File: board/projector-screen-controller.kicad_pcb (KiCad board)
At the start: 2 copper layers, 97.2 x 106 mm, 63 parts, among them J1 ICSP, J2 MSTBVA-3-G, J3 MCV-3-G, J4 MCV-3-G, J5 MCV-3-G, J6 MSTBVA-6-G, J7 MCV-3-G, K1 JS1-12V-F, K2 JS1-12V-F, K3 JS1-12V-F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

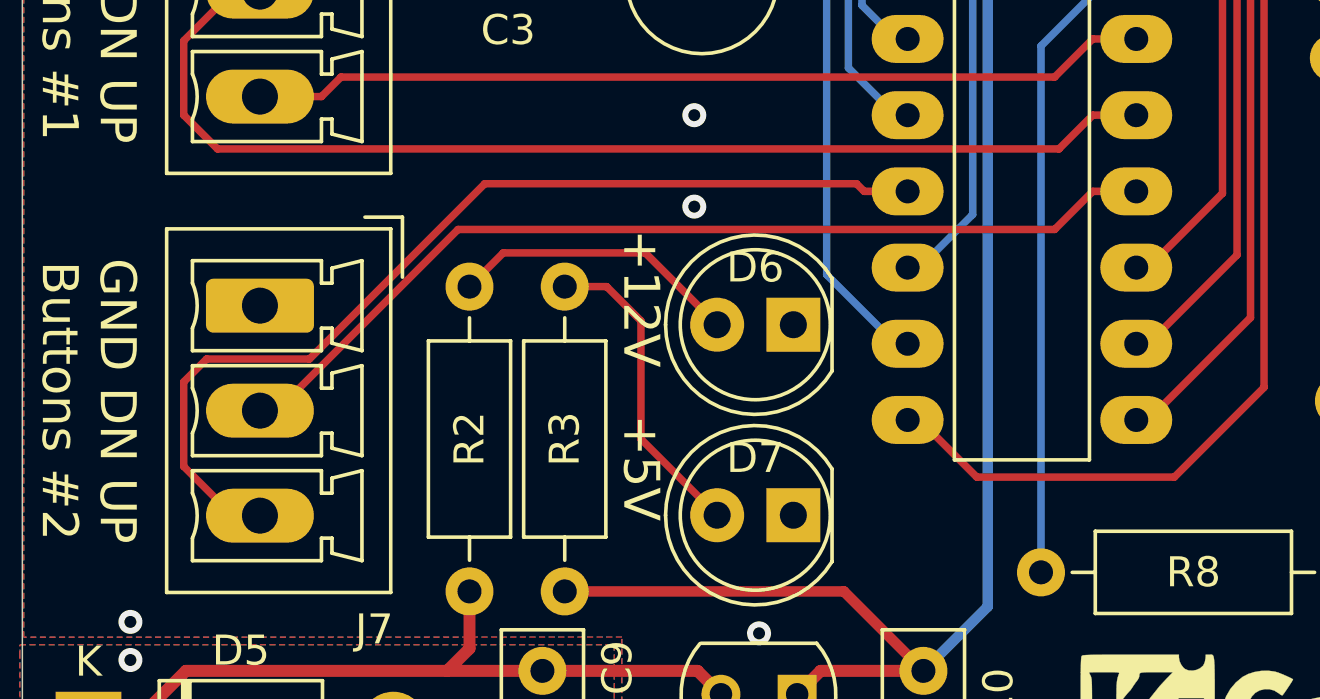
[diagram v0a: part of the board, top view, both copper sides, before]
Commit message: Fix channel 2 button reversal
* The hierarchical schematic pins for channel 2 buttons were reversed in the
  root schematic. Correct this, and add board revision logic to the firmware so
  board versions can be targeted by the build.
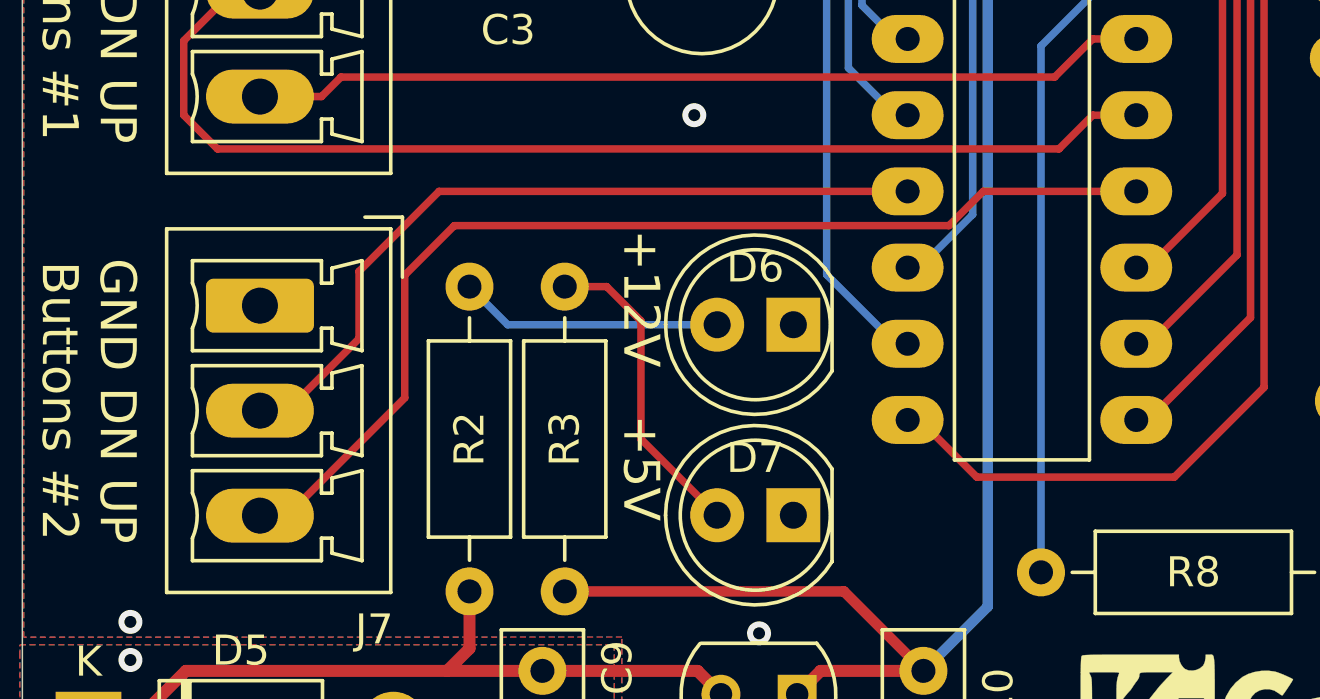
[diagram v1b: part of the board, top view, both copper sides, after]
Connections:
- J7 pad 2: /MCU/BUT2_UP -> /MCU/BUT2_DN
- J7 pad 3: /MCU/BUT2_DN -> /MCU/BUT2_UP
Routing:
- net /MCU/BUT2_DN: track 33.0 -> 25.9 mm
- net /MCU/BUT2_UP: track 32.2 -> 36.1 mm
- net Net-(D6-Pad2): track 9.71 -> 8.78 mm
- net GND: vias 12 -> 11
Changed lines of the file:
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@@
-(kicad_pcb (version 20171130) (host pcbnew "(5.1.4-0-10_14)")
+(kicad_pcb (version 20171130) (host pcbnew "(5.1.4)-1")
   (general
     (thickness 1.6)
     (drawings 91)
-    (tracks 381)
+    (tracks 377)
     (zones 0)
     (modules 63)
@@
   (title_block
     (title "Projector Screen Controller")
-    (date 2019-09-07)
+    (date 2019-09-13)
     (rev 0.2)
     (company "Flirble Open Source")
@@
     (fp_arc (start 0 3.95) (end -0.75 2.25) (angle 47.6) (layer F.SilkS) (width 0.12))
     (pad 3 thru_hole oval (at 7 0 270) (size 1.8 3.6) (drill 1.2) (layers *.Cu *.Mask)
-      (net 43 /MCU/BUT2_DN))
-    (pad 2 thru_hole oval (at 3.5 0 270) (size 1.8 3.6) (drill 1.2) (layers *.Cu *.Mask)
       (net 42 /MCU/BUT2_UP))
+    (pad 2 thru_hole oval (at 3.5 0 270) (size 1.8 3.6) (drill 1.2) (layers *.Cu *.Mask)
+      (net 43 /MCU/BUT2_DN))
     (pad 1 thru_hole roundrect (at 0 0 270) (size 1.8 3.6) (drill 1.2) (layers *.Cu *.Mask) (roundrect_rratio 0.138889)
       (net 2 GND))
@@
   (via (at 114.935 53.975) (size 0.8) (drill 0.4) (layers F.Cu B.Cu) (net 2))
   (via (at 104.14 80.01) (size 0.8) (drill 0.4) (layers F.Cu B.Cu) (net 2))
-  (via (at 97.028 99.568) (size 0.8) (drill 0.4) (layers F.Cu B.Cu) (net 2))
   (via (at 97.028 96.52) (size 0.8) (drill 0.4) (layers F.Cu B.Cu) (net 2))
   (segment (start 82.06 75.89) (end 82.13501 75.81499) (width 0.25) (layer B.Cu) (net 2) (status 30))
@@
   (segment (start 82.55 95.9) (end 84.6 95.9) (width 0.25) (layer F.Cu) (net 41) (status 10))
   (segment (start 84.6 95.9) (end 85.25 95.25) (width 0.25) (layer F.Cu) (net 41))
-  (segment (start 89.154 100.33) (end 109.04 100.33) (width 0.25) (layer F.Cu) (net 42))
-  (segment (start 109.04 100.33) (end 110.31 99.06) (width 0.25) (layer F.Cu) (net 42))
-  (segment (start 82.55 106.37) (end 83.114 106.37) (width 0.25) (layer F.Cu) (net 42) (status 30))
-  (segment (start 83.114 106.37) (end 89.154 100.33) (width 0.25) (layer F.Cu) (net 42) (status 10))
-  (segment (start 110.31 99.06) (end 111.76 99.06) (width 0.25) (layer F.Cu) (net 42) (status 20))
-  (segment (start 80.01 105.41) (end 80.772 104.648) (width 0.25) (layer F.Cu) (net 43))
-  (segment (start 80.772 104.648) (end 84.19959 104.648) (width 0.25) (layer F.Cu) (net 43))
-  (segment (start 102.69 99.06) (end 104.14 99.06) (width 0.25) (layer F.Cu) (net 43) (status 20))
-  (segment (start 84.19959 104.648) (end 90.04159 98.806) (width 0.25) (layer F.Cu) (net 43))
-  (segment (start 90.04159 98.806) (end 102.436 98.806) (width 0.25) (layer F.Cu) (net 43))
-  (segment (start 80.01 108.23) (end 80.01 105.41) (width 0.25) (layer F.Cu) (net 43))
-  (segment (start 82.55 109.87) (end 81.65 109.87) (width 0.25) (layer F.Cu) (net 43) (status 30))
-  (segment (start 102.436 98.806) (end 102.69 99.06) (width 0.25) (layer F.Cu) (net 43))
-  (segment (start 81.65 109.87) (end 80.01 108.23) (width 0.25) (layer F.Cu) (net 43) (status 10))
-  (segment (start 95.394999 101.109999) (end 97.79 103.505) (width 0.25) (layer F.Cu) (net 51) (status 20))
-  (segment (start 90.660001 101.109999) (end 95.394999 101.109999) (width 0.25) (layer F.Cu) (net 51))
-  (segment (start 89.535 102.235) (end 90.660001 101.109999) (width 0.25) (layer F.Cu) (net 51) (status 10))
+  (segment (start 83.45 109.87) (end 82.55 109.87) (width 0.25) (layer F.Cu) (net 42))
+  (segment (start 111.76 99.06) (end 106.659502 99.06) (width 0.25) (layer F.Cu) (net 42))
+  (segment (start 105.516502 100.203) (end 89.027 100.203) (width 0.25) (layer F.Cu) (net 42))
+  (segment (start 89.027 100.203) (end 87.376 101.854) (width 0.25) (layer F.Cu) (net 42))
+  (segment (start 87.376 101.854) (end 87.376 105.944) (width 0.25) (layer F.Cu) (net 42))
+  (segment (start 106.659502 99.06) (end 105.516502 100.203) (width 0.25) (layer F.Cu) (net 42))
+  (segment (start 87.376 105.944) (end 83.45 109.87) (width 0.25) (layer F.Cu) (net 42))
+  (segment (start 83.45 106.37) (end 82.55 106.37) (width 0.25) (layer F.Cu) (net 43))
+  (segment (start 85.852 103.968) (end 83.45 106.37) (width 0.25) (layer F.Cu) (net 43))
+  (segment (start 85.852 101.727) (end 85.852 103.968) (width 0.25) (layer F.Cu) (net 43))
+  (segment (start 104.14 99.06) (end 88.519 99.06) (width 0.25) (layer F.Cu) (net 43))
+  (segment (start 88.519 99.06) (end 85.852 101.727) (width 0.25) (layer F.Cu) (net 43))
+  (segment (start 90.805 103.505) (end 89.535 102.235) (width 0.25) (layer B.Cu) (net 51))
+  (segment (start 97.79 103.505) (end 90.805 103.505) (width 0.25) (layer B.Cu) (net 51))
   (segment (start 95.25 107.315) (end 97.79 109.855) (width 0.25) (layer F.Cu) (net 52) (status 20))
   (segment (start 95.25 103.378) (end 95.25 107.315) (width 0.25) (layer F.Cu) (net 52))

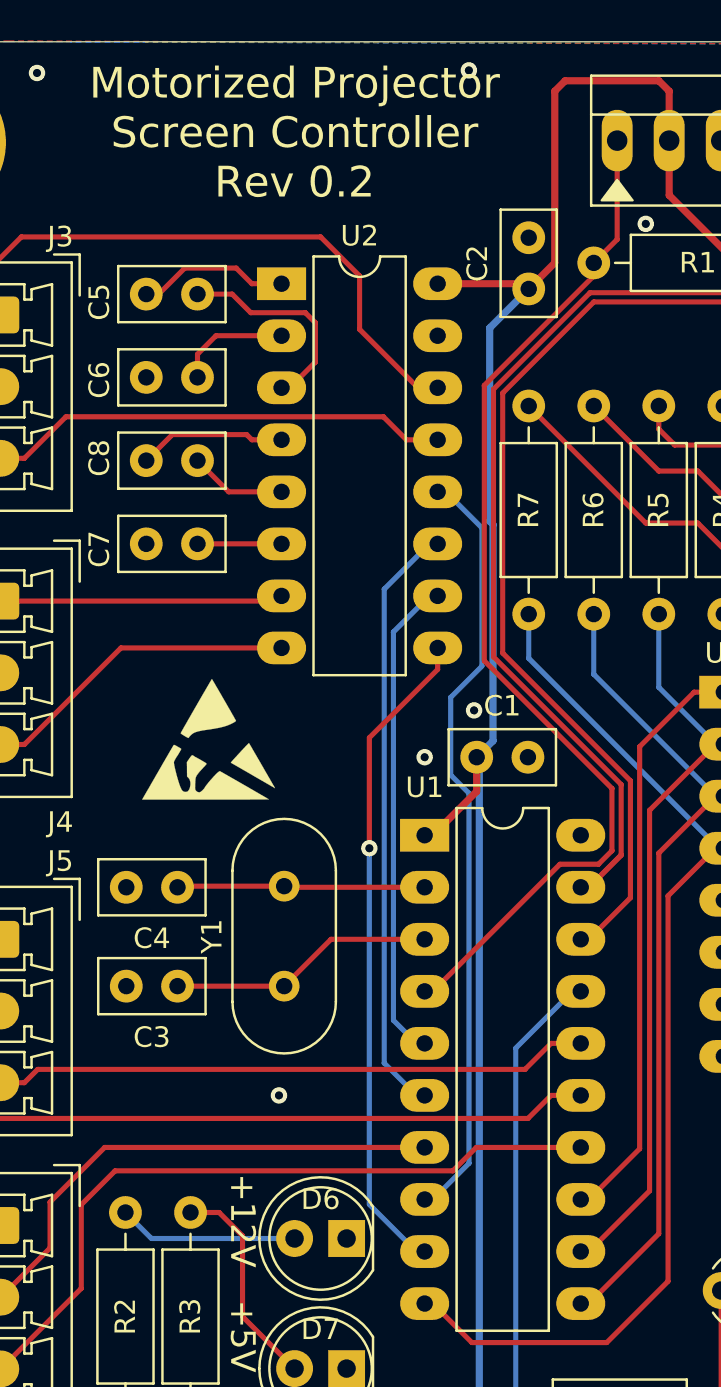
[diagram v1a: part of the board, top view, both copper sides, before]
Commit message: Update gerbers; minor layout tweaks
* Add ICSP text next to ISCP header
* Better spacing around channel 2 button traces
* Update 3d preview, gerbers and board PDF
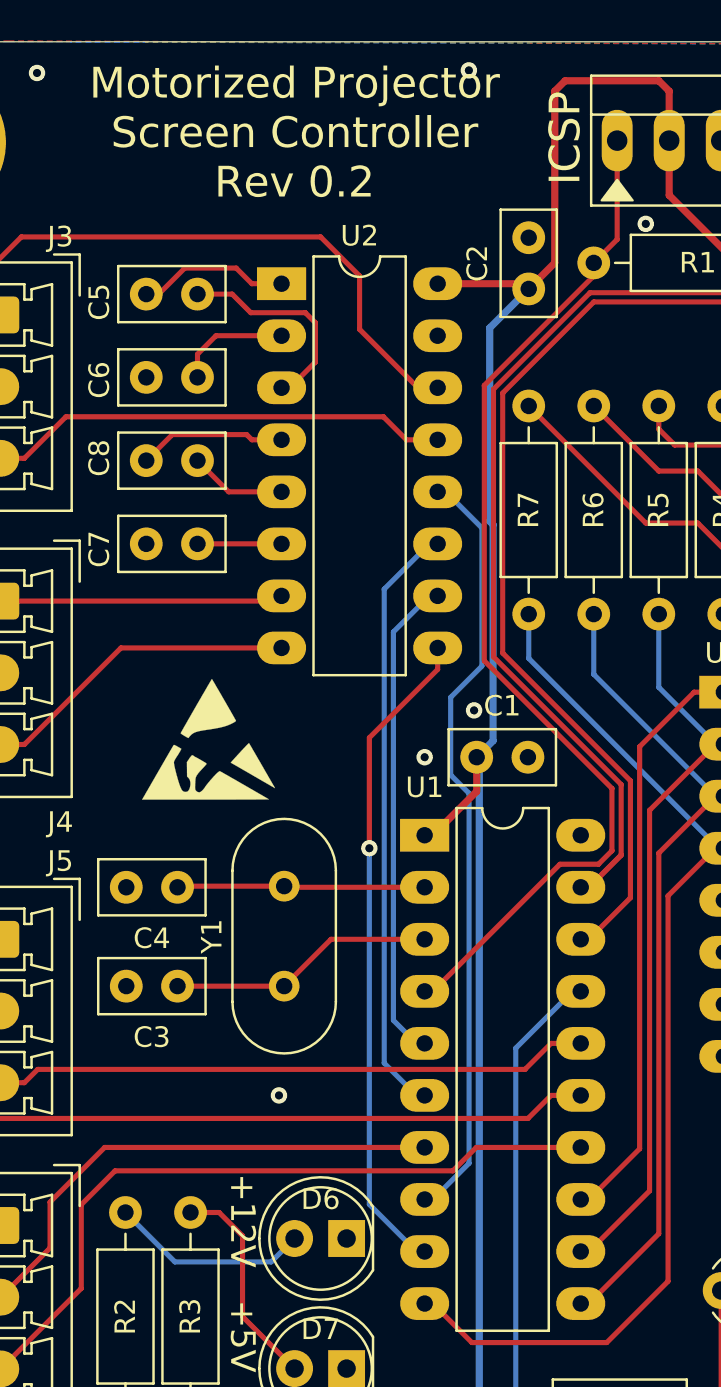
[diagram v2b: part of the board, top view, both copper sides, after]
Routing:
- net Net-(D6-Pad2): track 8.78 -> 9.73 mm
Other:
- board text added: "ICSP"
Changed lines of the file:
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@@
   (general
     (thickness 1.6)
-    (drawings 91)
-    (tracks 377)
+    (drawings 90)
+    (tracks 378)
     (zones 0)
     (modules 63)
@@
     )
   )
+  (gr_text ICSP (at 110.998 49.784 90) (layer F.SilkS)
+    (effects (font (size 1.5 1.5) (thickness 0.2)))
+  )
   (gr_line (start 161.671 113.792) (end 162.941 110.998) (layer F.SilkS) (width 0.4))
   (gr_line (start 163.195 112.903) (end 161.671 113.792) (layer F.SilkS) (width 0.4))
@@
   (gr_line (start 135.255 50.165) (end 135.255 57.785) (layer Edge.Cuts) (width 0.1))
   (gr_line (start 74.63 45.085) (end 171.785 45.085) (layer Edge.Cuts) (width 0.05))
-  (gr_circle (center 80 144.5) (end 81.9 144.5) (layer Eco1.User) (width 0.05))
-  (gr_circle (center 80 50) (end 81.9 50) (layer Eco1.User) (width 0.05))
   (gr_line (start 74.63 151.13) (end 74.63 45.085) (layer Edge.Cuts) (width 0.05))
   (gr_line (start 171.785 151.13) (end 74.63 151.13) (layer Edge.Cuts) (width 0.05))
@@
   (segment (start 104.14 99.06) (end 88.519 99.06) (width 0.25) (layer F.Cu) (net 43))
   (segment (start 88.519 99.06) (end 85.852 101.727) (width 0.25) (layer F.Cu) (net 43))
-  (segment (start 90.805 103.505) (end 89.535 102.235) (width 0.25) (layer B.Cu) (net 51))
-  (segment (start 97.79 103.505) (end 90.805 103.505) (width 0.25) (layer B.Cu) (net 51))
+  (segment (start 91.948 104.648) (end 89.535 102.235) (width 0.25) (layer B.Cu) (net 51))
+  (segment (start 97.79 103.505) (end 96.647 104.648) (width 0.25) (layer B.Cu) (net 51))
+  (segment (start 96.647 104.648) (end 91.948 104.648) (width 0.25) (layer B.Cu) (net 51))
   (segment (start 95.25 107.315) (end 97.79 109.855) (width 0.25) (layer F.Cu) (net 52) (status 20))
   (segment (start 95.25 103.378) (end 95.25 107.315) (width 0.25) (layer F.Cu) (net 52))

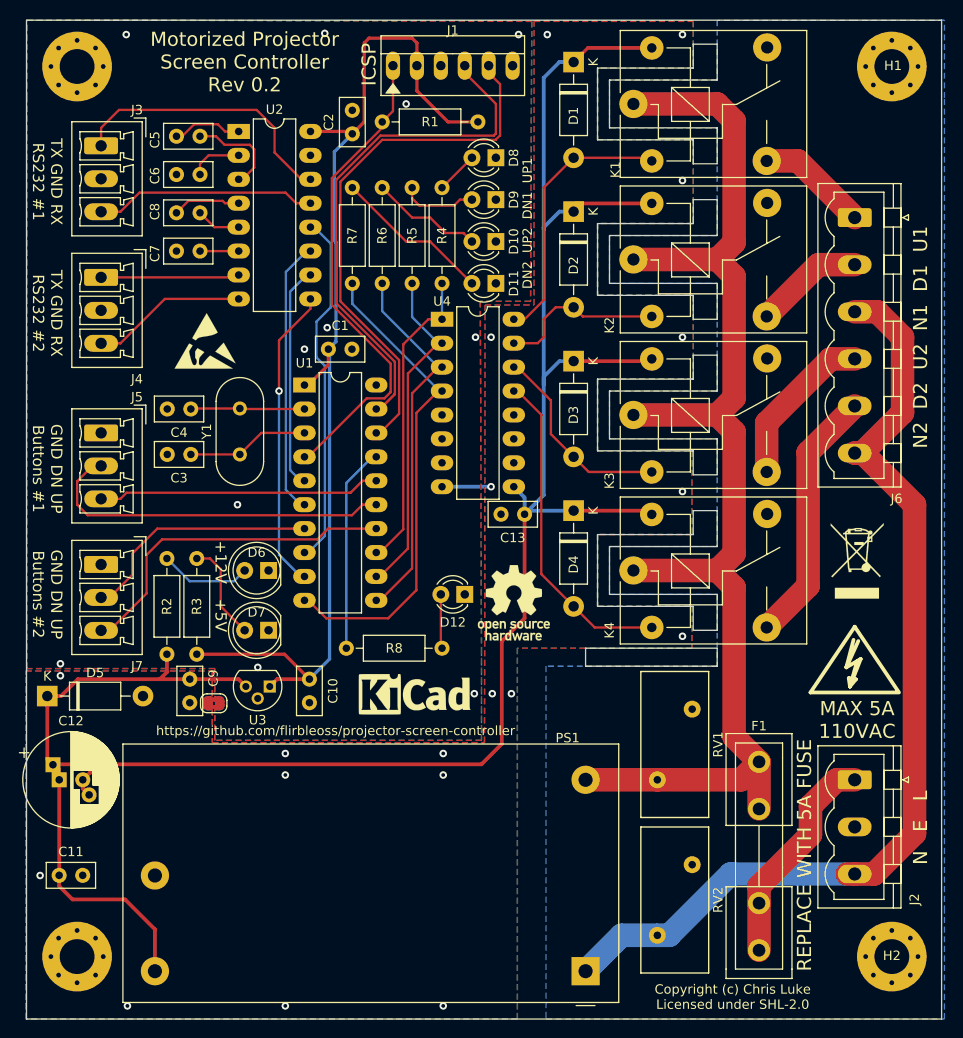
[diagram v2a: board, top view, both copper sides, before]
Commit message: Adjust ground plane clearance, LED margin clearances
* For PCB DRC checks, fix clearances.
* Make AC section tracks slightly larger.
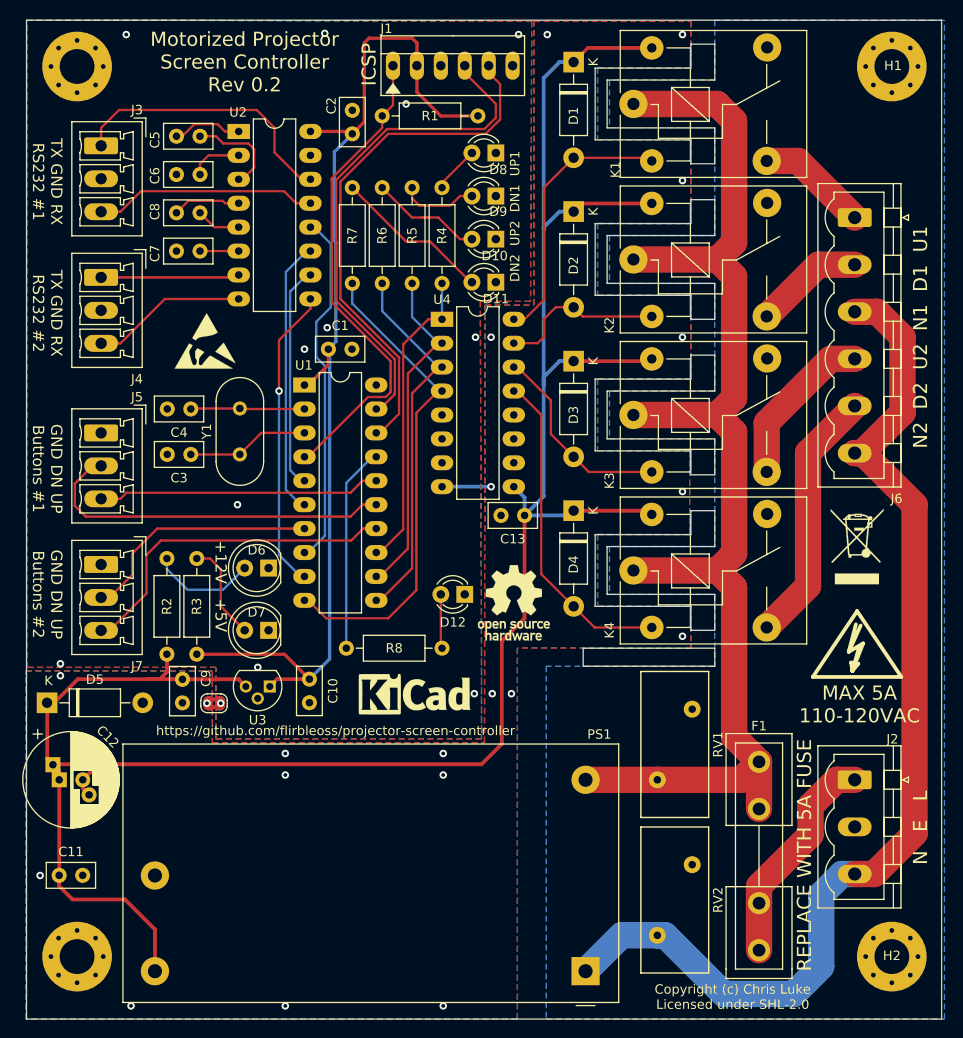
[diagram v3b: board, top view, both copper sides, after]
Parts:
- moved REF*** 1.52 mm to (162.8, 101.0)
- moved C9 0.78 mm to (91.2, 115.1)
- moved D5 0.71 mm to (76.8, 117.6)
- moved R1 0.64 mm to (122.6, 55.2)
- moved D8 0.51 mm to (124.5, 59.2)
- moved D9 0.38 mm to (124.5, 63.8)
- moved D10 0.25 mm to (124.5, 68.3)
- moved D6 0.25 mm to (100.3, 103.3)
- moved D11 0.13 mm to (124.5, 72.9)
- moved C13 0.13 mm to (127.5, 97.7)
- moved JP2 0.08 mm to (94.6, 117.6)
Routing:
- net NEUT: track 106.4 -> 115.2 mm
- net +12V: track 239.0 -> 241.3 mm
- net Net-(D6-Pad2): track 9.73 -> 11.2 mm
- net Net-(J1-Pad5): track 57.4 -> 56.4 mm
- net Net-(J1-Pad4): track 57.8 -> 56.8 mm
- net Net-(D10-Pad2): track 11.9 -> 12.7 mm
- net /MCU/BUT1_DN: track 38.4 -> 38.9 mm
- net Net-(D8-Pad2): track 4.49 -> 5.00 mm
- net GNDPWR: vias 20 -> 21
- net GND: vias 11 -> 12
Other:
- outline, holes or cut-outs redrawn
- net class AC Power: clearance 0.5 -> 0.45; trace_width 2.5 -> 2.8
- rule trace_min: 0.2 -> 0.127
- board text added: "MAX 5A 110-120VAC"
- board text removed: "MAX 5A 110VAC"
